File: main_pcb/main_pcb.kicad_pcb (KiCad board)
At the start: 2 copper layers, 95 x 95 mm, 54 parts, among them J1 DBG, J2 UI, J3 UI, J4 Raspberry_Pi_Zero_WH, J5 UI, J6 UI, J7 UPDN, J8 ISP, J9 BTN_TRIG, Q1 BSS123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

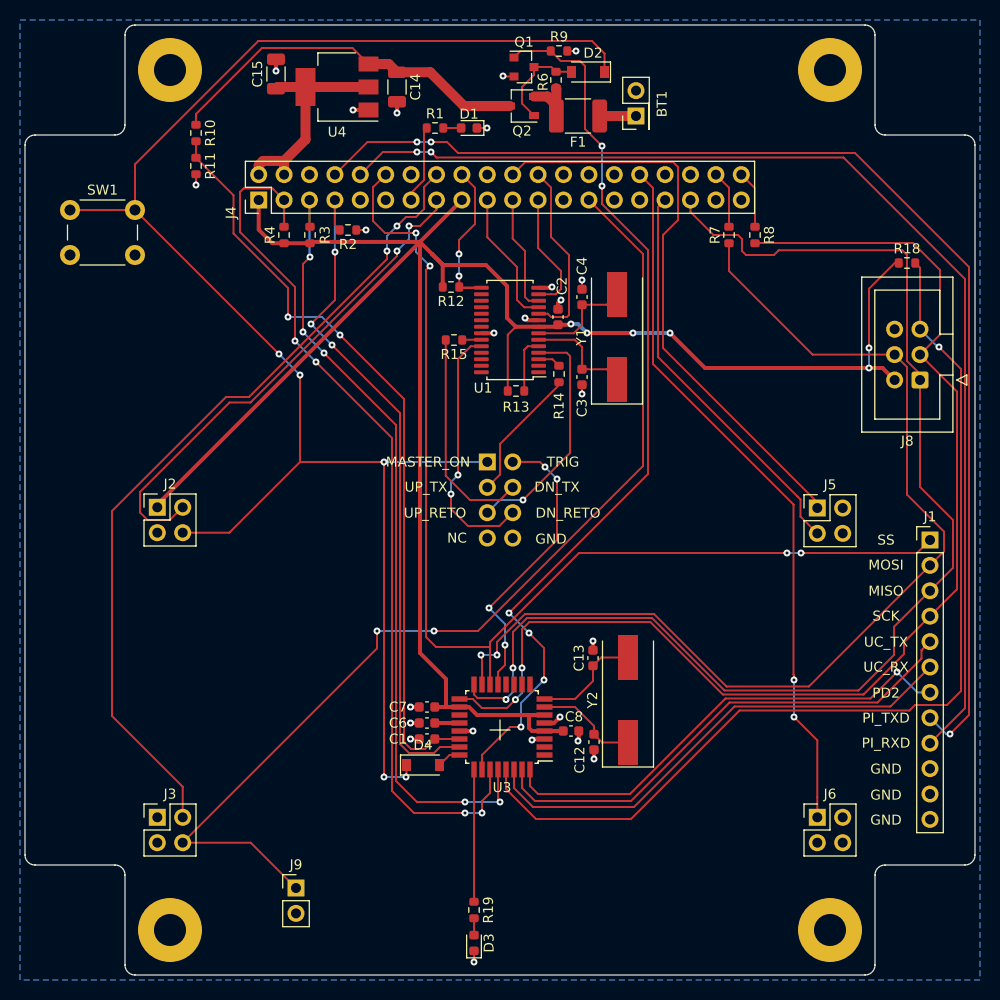
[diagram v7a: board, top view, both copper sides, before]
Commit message: Merged PCBs to KiCAD 6 format
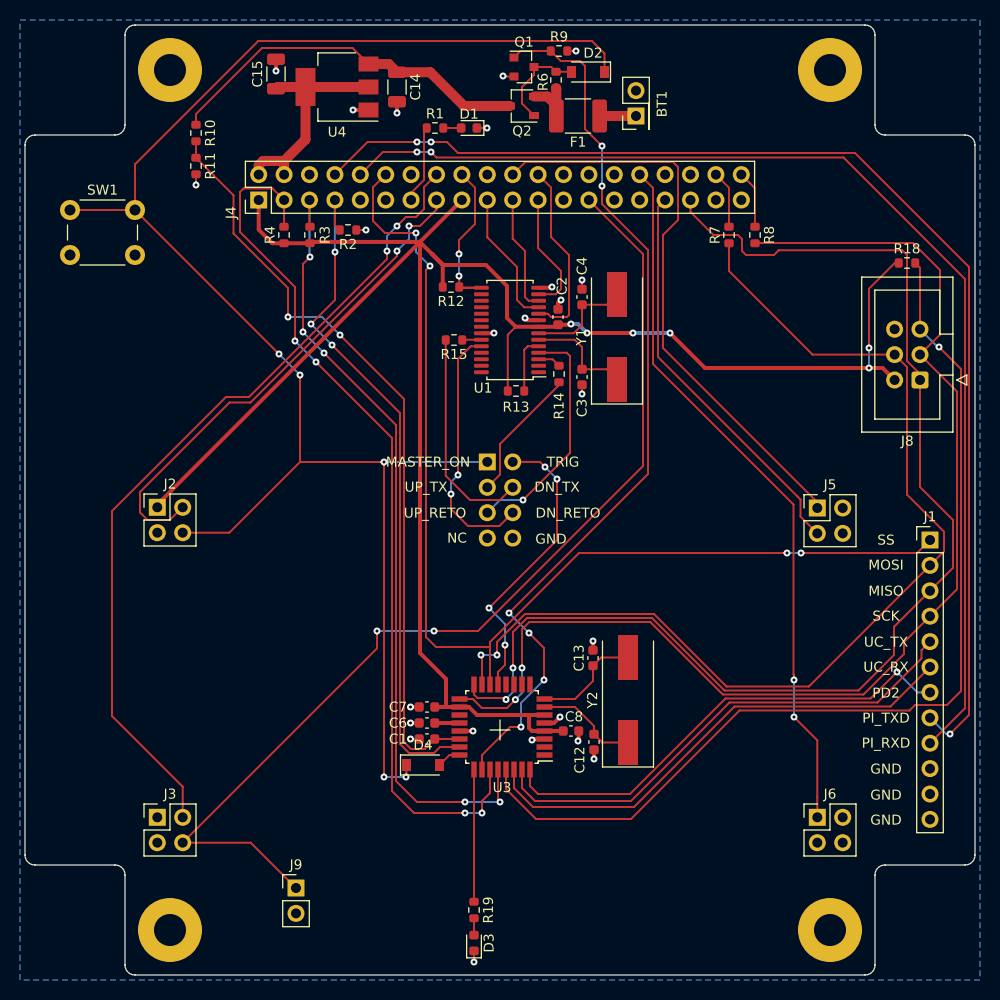
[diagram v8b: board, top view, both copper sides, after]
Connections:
- net /~RESET renamed /~{RESET}
- net /~SC_IRQ renamed /~{SC_IRQ}
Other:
- net class Default removed
